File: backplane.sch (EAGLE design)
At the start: 14 parts, among them IC1 MAX3233ECWP

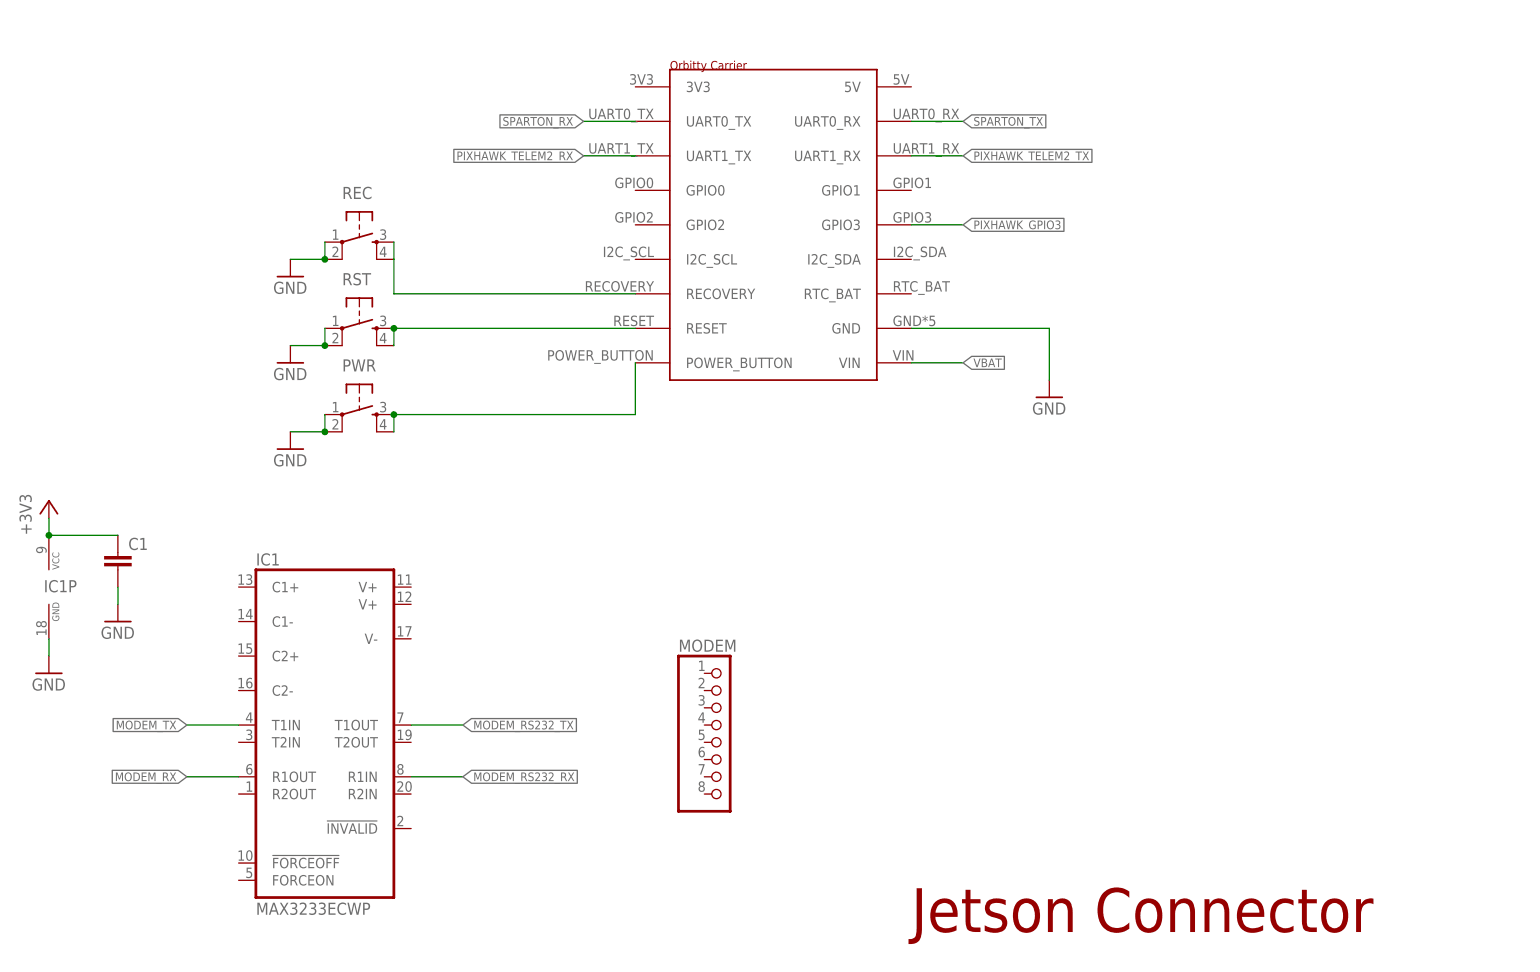
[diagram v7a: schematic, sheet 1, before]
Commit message: Add jetson - converter uart connection
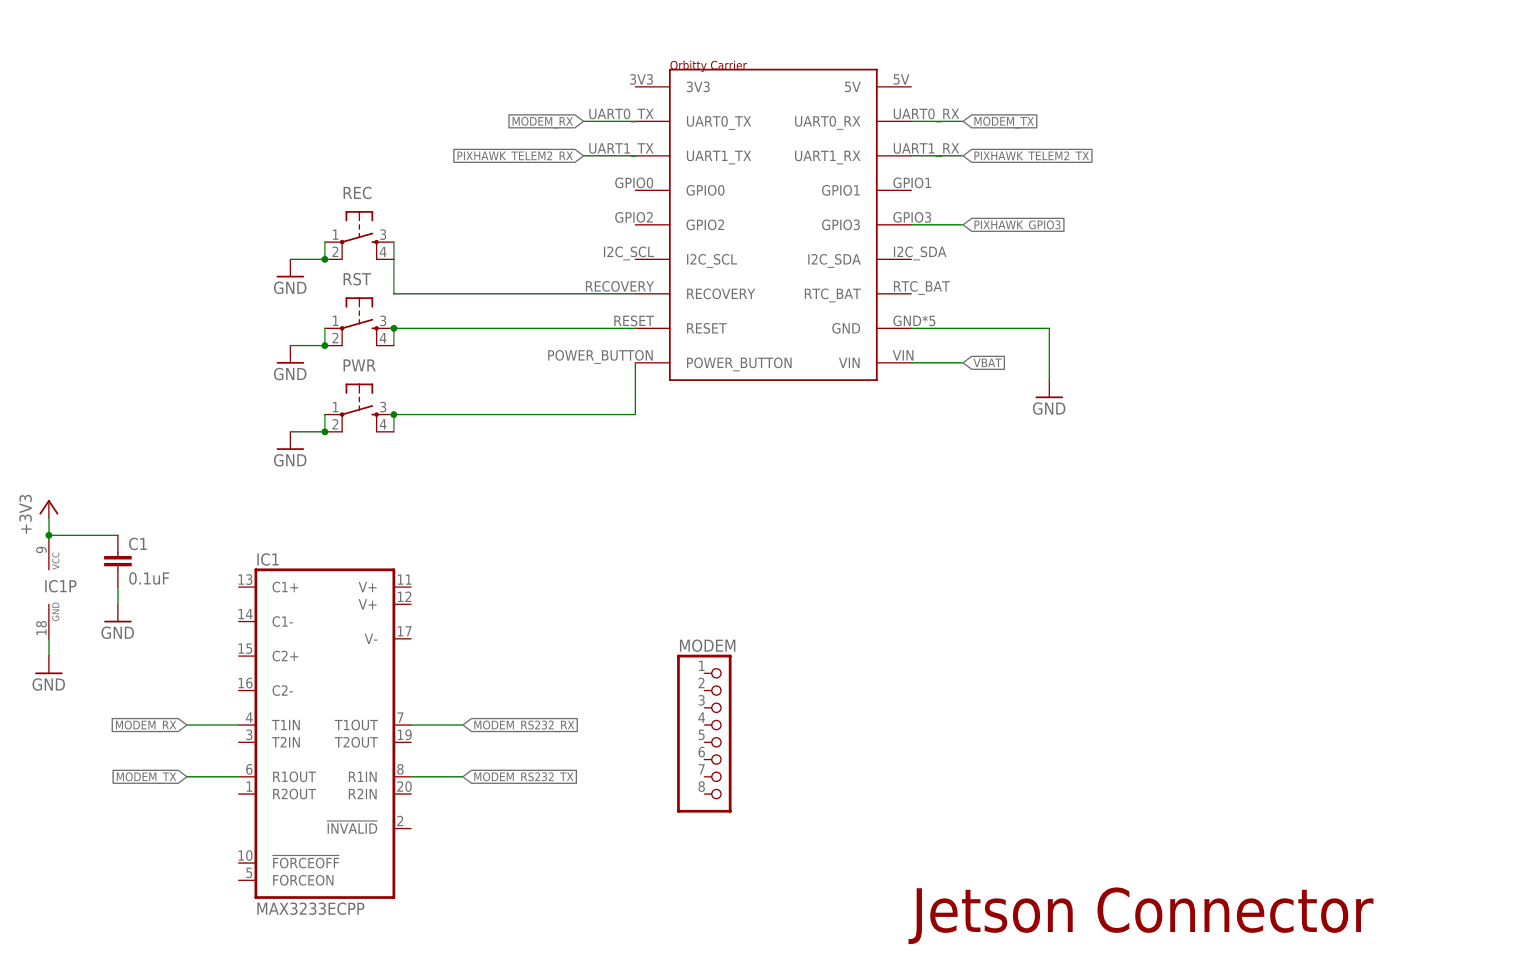
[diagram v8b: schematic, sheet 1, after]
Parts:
- C1: value (none) -> 0.1uF
- IC1: value MAX3233ECWP -> MAX3233ECPP; device auv:MAX3233ECWP -> auv:MAX3233ECPP
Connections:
- removed net SPARTON_RX: U$3.UART0_TX
- removed net SPARTON_TX: U$3.UART0_RX
- net MODEM_RS232_RX: now also IC1Q.T1OUT; no longer IC1Q.R1IN
- net MODEM_RS232_TX: now also IC1Q.R1IN; no longer IC1Q.T1OUT
- net MODEM_RX: now also IC1Q.T1IN, U$3.UART0_TX; no longer IC1Q.R1OUT
- net MODEM_TX: now also IC1Q.R1OUT, U$3.UART0_RX; no longer IC1Q.T1IN
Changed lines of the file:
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@@
 <part name="P+3" library="auv" deviceset="+5V" device=""/>
 <part name="MODEM" library="auv" deviceset="PINHD-1X8" device=""/>
-<part name="IC1" library="auv" deviceset="MAX3233E" device="WP" technology="C"/>
+<part name="IC1" library="auv" deviceset="MAX3233E" device="PP" technology="C" value="MAX3233ECPP"/>
 <part name="+3V1" library="auv" deviceset="+3V3" device=""/>
 <part name="GND11" library="auv" deviceset="GND" device=""/>
-<part name="C1" library="auv" deviceset="C-EU" device="C0603"/>
+<part name="C1" library="auv" deviceset="C-EU" device="C0603" value="0.1uF"/>
 <part name="GND12" library="auv" deviceset="GND" device=""/>
 </parts>
@@
 </segment>
 </net>
-<net name="SPARTON_RX" class="0">
-<segment>
-<pinref part="U$3" gate="G$1" pin="UART0_TX"/>
-<wire x1="134.62" y1="144.78" x2="127" y2="144.78" width="0.1524" layer="91"/>
-<label x="127" y="144.78" size="1.27" layer="95" rot="R180" xref="yes"/>
-</segment>
-</net>
 <net name="PWR" class="0">
 <segment>
@@
 </segment>
 </net>
-<net name="SPARTON_TX" class="0">
-<segment>
-<pinref part="U$3" gate="G$1" pin="UART0_RX"/>
-<wire x1="175.26" y1="144.78" x2="182.88" y2="144.78" width="0.1524" layer="91"/>
-<label x="182.88" y="144.78" size="1.27" layer="95" xref="yes"/>
-</segment>
-</net>
 <net name="PIXHAWK_GPIO3" class="0">
 <segment>
@@
 </segment>
 </net>
-<net name="MODEM_RS232_TX" class="0">
+<net name="MODEM_RS232_RX" class="0">
 <segment>
 <pinref part="IC1" gate="Q" pin="T1OUT"/>
@@
 </segment>
 </net>
-<net name="MODEM_RS232_RX" class="0">
+<net name="MODEM_RX" class="0">
 <segment>
-<pinref part="IC1" gate="Q" pin="R1IN"/>
-<wire x1="101.6" y1="48.26" x2="109.22" y2="48.26" width="0.1524" layer="91"/>
-<label x="109.22" y="48.26" size="1.27" layer="95" xref="yes"/>
+<pinref part="U$3" gate="G$1" pin="UART0_TX"/>
+<wire x1="134.62" y1="144.78" x2="127" y2="144.78" width="0.1524" layer="91"/>
+<label x="127" y="144.78" size="1.27" layer="95" rot="R180" xref="yes"/>
 </segment>
-</net>
-<net name="MODEM_TX" class="0">
 <segment>
 <pinref part="IC1" gate="Q" pin="T1IN"/>
 <wire x1="76.2" y1="55.88" x2="68.58" y2="55.88" width="0.1524" layer="91"/>
 <label x="68.58" y="55.88" size="1.27" layer="95" rot="R180" xref="yes"/>
-</segment>
-</net>
-<net name="MODEM_RX" class="0">
-<segment>
-<pinref part="IC1" gate="Q" pin="R1OUT"/>
-<wire x1="76.2" y1="48.26" x2="68.58" y2="48.26" width="0.1524" layer="91"/>
-<label x="68.58" y="48.26" size="1.27" layer="95" rot="R180" xref="yes"/>
 </segment>
 </net>
@@
 </segment>
 </net>
+<net name="MODEM_RS232_TX" class="0">
+<segment>
+<pinref part="IC1" gate="Q" pin="R1IN"/>
+<wire x1="101.6" y1="48.26" x2="109.22" y2="48.26" width="0.1524" layer="91"/>
+<label x="109.22" y="48.26" size="1.27" layer="95" xref="yes"/>
+</segment>
+</net>
+<net name="MODEM_TX" class="0">
+<segment>
+<pinref part="IC1" gate="Q" pin="R1OUT"/>
+<wire x1="76.2" y1="48.26" x2="68.58" y2="48.26" width="0.1524" layer="91"/>
+<label x="68.58" y="48.26" size="1.27" layer="95" rot="R180" xref="yes"/>
+</segment>
+<segment>
+<pinref part="U$3" gate="G$1" pin="UART0_RX"/>
+<wire x1="175.26" y1="144.78" x2="182.88" y2="144.78" width="0.1524" layer="91"/>
+<label x="182.88" y="144.78" size="1.27" layer="95" xref="yes"/>
+</segment>
+</net>
